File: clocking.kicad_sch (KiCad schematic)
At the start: 10 parts, among them J14 LOCTL, J15 RAMPCTL, Q1 DTC143Z

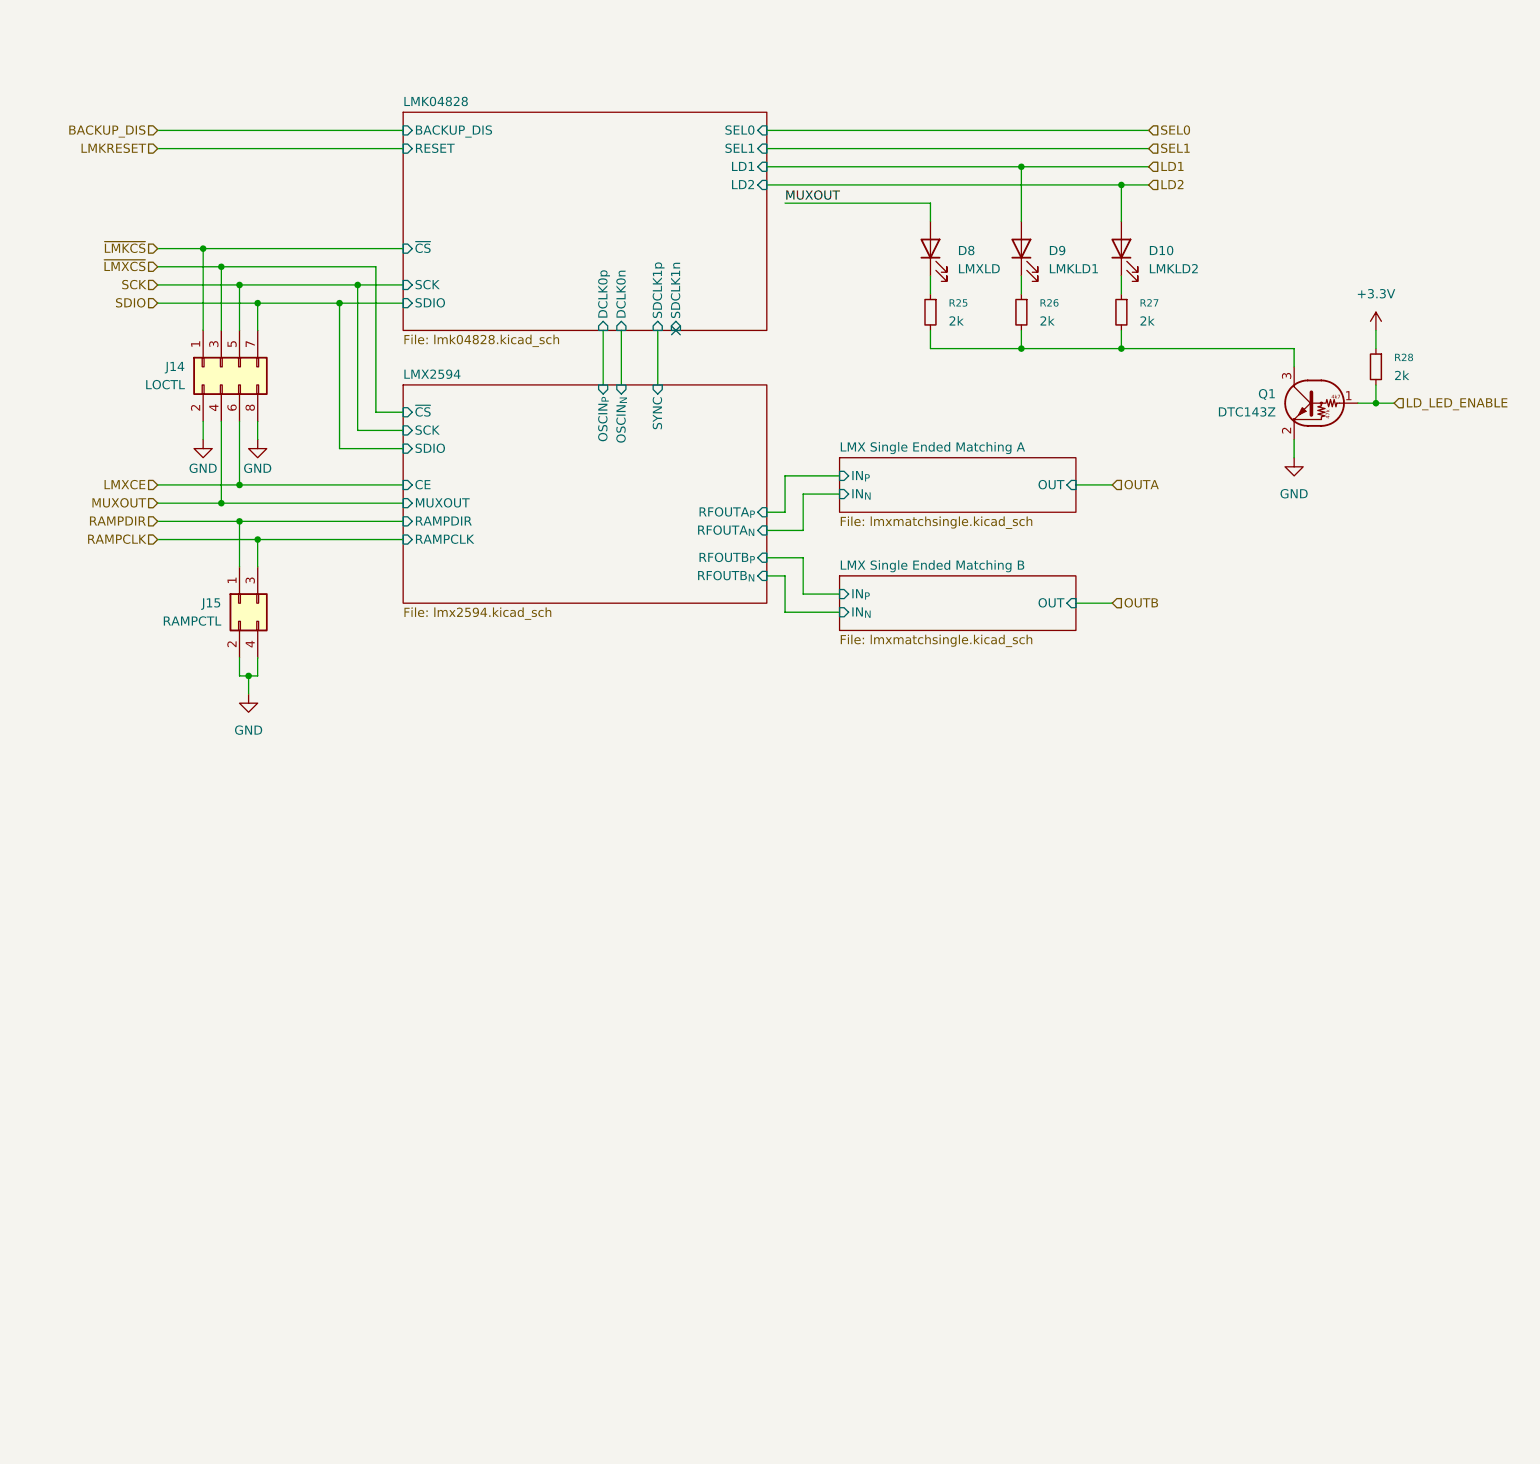
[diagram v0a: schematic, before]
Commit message: Add Clock sources and monitor output
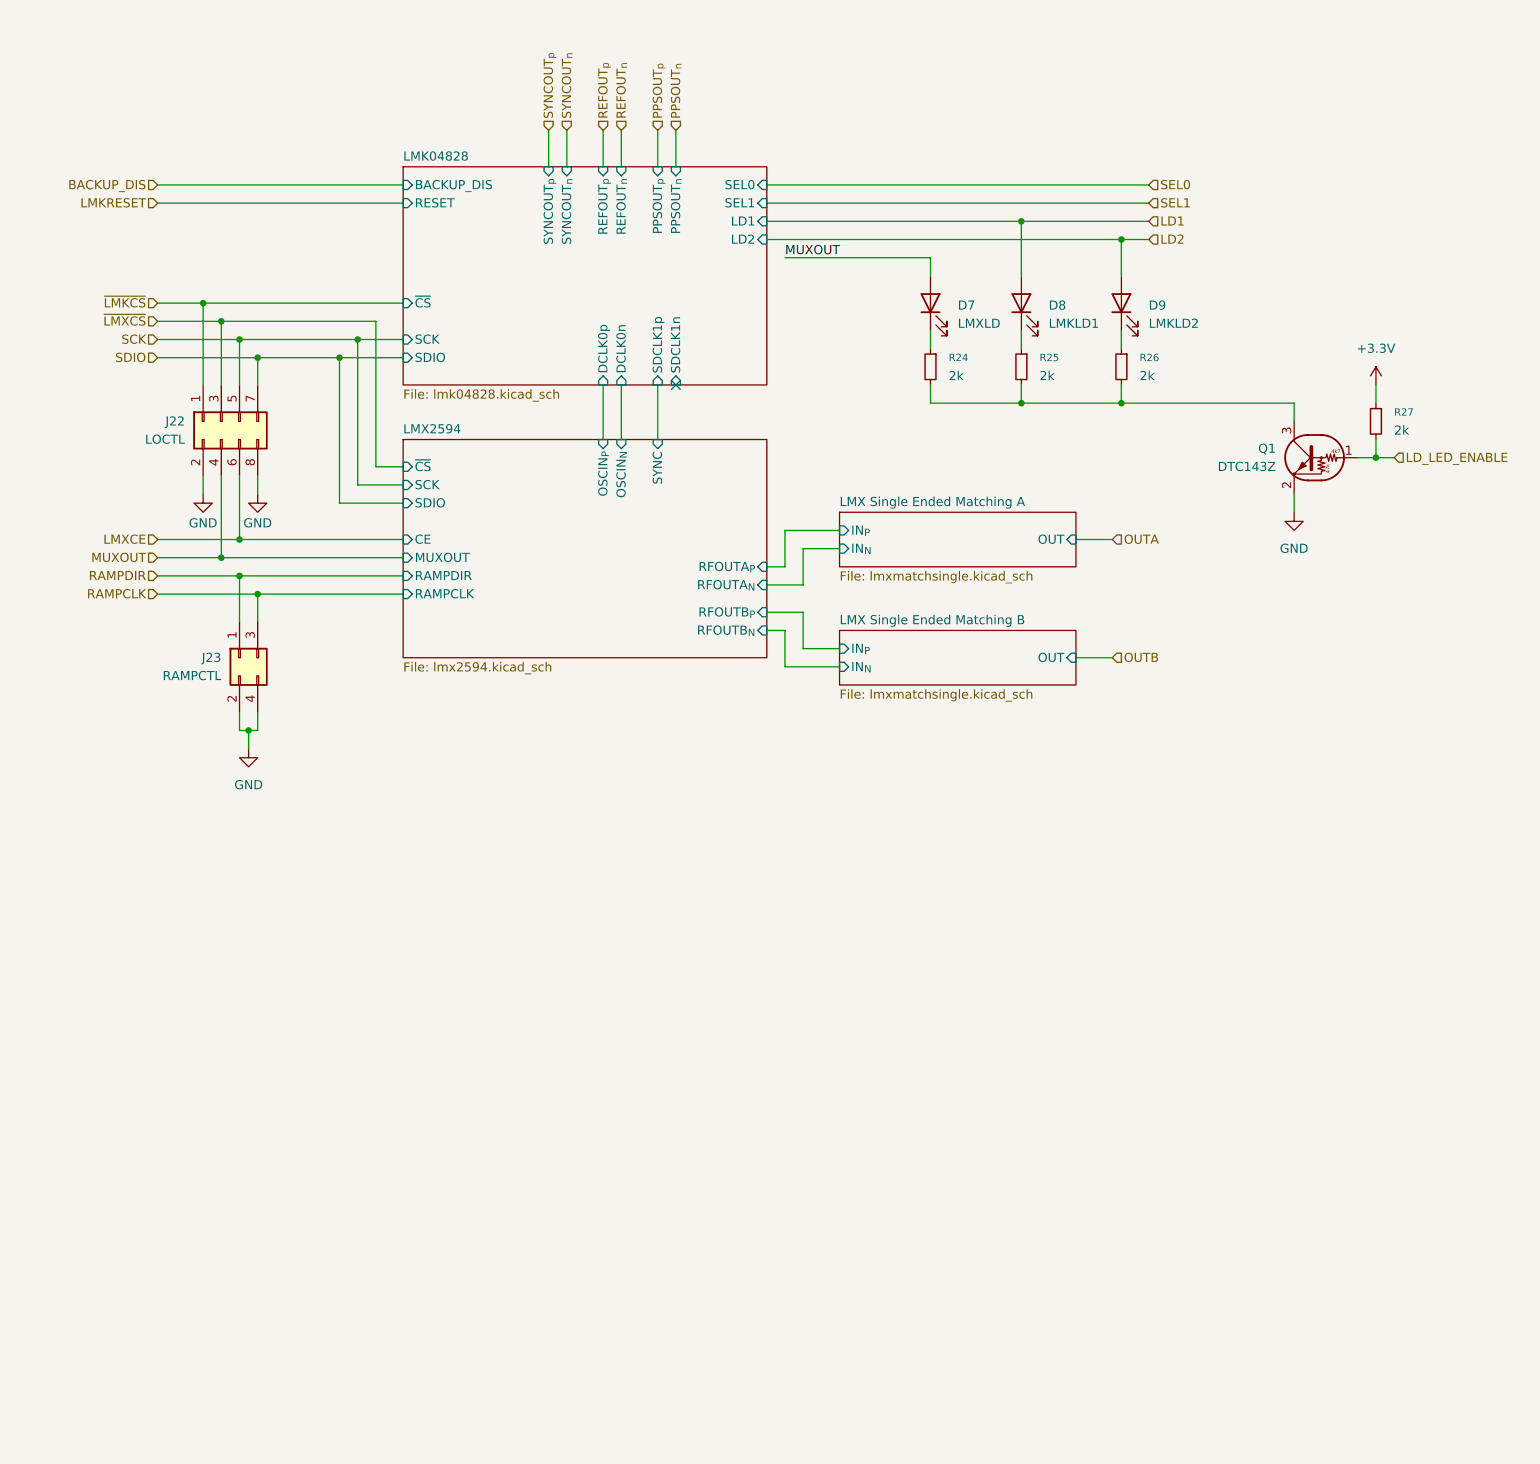
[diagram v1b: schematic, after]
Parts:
- renumbered D8 to D7, D9 to D8, D10 to D9, J14 to J22, J15 to J23, R25 to R24, R26 to R25, R27 to R26, R28 to R27
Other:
- sheet LMK04828 ports: added PPSOUT_{n}, PPSOUT_{p}, REFOUT_{n}, REFOUT_{p}, SYNCOUT_{n}, SYNCOUT_{p}; removed none
- moved on the sheet: D7, D8, D9, J22, J23, Q1, R24, R25, R26, R27

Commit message: Round 1 review comments
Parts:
- renumbered J22 to J23, J23 to J24, R24 to R52, R25 to R53, R26 to R54, R27 to R55
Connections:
- no-connect marks 1 -> 5
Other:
- added sheet LMX Single Ended Matching A1 (lmxmatchsingle.kicad_sch)
- added sheet LMX2595 (lmx2594.kicad_sch)
- sheet LMK04828 ports: added DCLK2n, DCLK2p, SDCLK3n, SDCLK3p; removed none
- sheet LMX Single Ended Matching A ports: added +3.3VA_LMXBUF; removed none
- sheet LMX Single Ended Matching B ports: added +3.3VA_LMXBUF; removed none
- sheet LMX2594 ports: added +3.3VA_LMXBUF; removed none
- moved on the sheet: D7, D8, D9, J23, J24, Q1, R52, R53, R54, R55

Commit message: Round 2 Review, power tree cleanup
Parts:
- renumbered J23 to J24, J24 to J25, R52 to R62, R53 to R63, R54 to R64, R55 to R65
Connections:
- no-connect marks 5 -> 6

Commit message: Darrel Suggestions
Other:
- note added: "10-12GHz"
- note added: "5-7GHZ"
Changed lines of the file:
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@@
 	(generator_version "10.0")
 	(paper "A3")
+	(text "10-12GHz"
+		(exclude_from_sim no)
+		(at 171.45 71.374 0)
+		(effects
+			(font
+				(size 1.27 1.27)
+			)
+		)
+	)
+	(text "5-7GHZ"
+		(exclude_from_sim no)
+		(at 168.656 190.754 0)
+		(effects
+			(font
+				(size 1.27 1.27)
+			)
+		)
+	)
+	(text "5-7GHZ"
+		(exclude_from_sim no)
+		(at 168.656 170.434 0)
+		(effects
+			(font
+				(size 1.27 1.27)
+			)
+		)
+	)
 	(junction
 		(at 162.56 180.34)
@@
 		(dnp no)
 		(fields_autoplaced yes)
-		(property "Reference" "#PWR095"
+		(property "Reference" "#PWR097"
 			(at 190.5 181.61 0)
 			(hide yes)
@@
 			(project "huskypointofload"
 				(path "/eb9c972b-d134-41da-be97-ece3f463f7e0/999a5927-21bb-4ea7-ad27-c6446933693a"
-					(reference "#PWR095")
+					(reference "#PWR097")
 					(unit 1)
 				)
@@
 		(in_pos_files yes)
 		(dnp no)
-		(property "Reference" "#PWR092"
+		(property "Reference" "#PWR094"
 			(at 38.1 179.07 0)
 			(hide yes)
@@
 			(project "huskypointofload"
 				(path "/eb9c972b-d134-41da-be97-ece3f463f7e0/999a5927-21bb-4ea7-ad27-c6446933693a"
-					(reference "#PWR092")
+					(reference "#PWR094")
 					(unit 1)
 				)
@@
 		(dnp no)
 		(fields_autoplaced yes)
-		(property "Reference" "#PWR093"
+		(property "Reference" "#PWR095"
 			(at 44.45 214.63 0)
 			(hide yes)
@@
 			(project "huskypointofload"
 				(path "/eb9c972b-d134-41da-be97-ece3f463f7e0/999a5927-21bb-4ea7-ad27-c6446933693a"
-					(reference "#PWR093")
+					(reference "#PWR095")
 					(unit 1)
 				)
@@
 		(in_pos_files yes)
 		(dnp no)
-		(property "Reference" "#PWR094"
+		(property "Reference" "#PWR096"
 			(at 45.72 179.07 0)
 			(hide yes)
@@
 			(project "huskypointofload"
 				(path "/eb9c972b-d134-41da-be97-ece3f463f7e0/999a5927-21bb-4ea7-ad27-c6446933693a"
-					(reference "#PWR094")
+					(reference "#PWR096")
 					(unit 1)
 				)
@@
 		(dnp no)
 		(fields_autoplaced yes)
-		(property "Reference" "#PWR096"
+		(property "Reference" "#PWR098"
 			(at 201.93 161.29 0)
 			(hide yes)
@@
 			(project "huskypointofload"
 				(path "/eb9c972b-d134-41da-be97-ece3f463f7e0/999a5927-21bb-4ea7-ad27-c6446933693a"
-					(reference "#PWR096")
+					(reference "#PWR098")
 					(unit 1)
 				)

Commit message: Passive footprint pass
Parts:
- D7, D8, D9: footprint (none) -> LED_SMD:LED_0402_1005Metric
- R62, R63, R64, R65: footprint (none) -> Resistor_SMD:R_0402_1005Metric
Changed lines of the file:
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@@
 			)
 		)
-		(property "Footprint" ""
+		(property "Footprint" "LED_SMD:LED_0402_1005Metric"
 			(at 139.7 146.05 0)
 			(hide yes)
@@
 			)
 		)
-		(property "Footprint" ""
+		(property "Footprint" "Resistor_SMD:R_0402_1005Metric"
 			(at 139.7 154.94 0)
 			(hide yes)
@@
 			)
 		)
-		(property "Footprint" ""
+		(property "Footprint" "Resistor_SMD:R_0402_1005Metric"
 			(at 166.37 154.94 0)
 			(hide yes)
@@
 			)
 		)
-		(property "Footprint" ""
+		(property "Footprint" "LED_SMD:LED_0402_1005Metric"
 			(at 166.37 146.05 0)
 			(hide yes)
@@
 			)
 		)
-		(property "Footprint" ""
+		(property "Footprint" "LED_SMD:LED_0402_1005Metric"
 			(at 152.4 146.05 0)
 			(hide yes)
@@
 			)
 		)
-		(property "Footprint" ""
+		(property "Footprint" "Resistor_SMD:R_0402_1005Metric"
 			(at 201.93 162.56 0)
 			(hide yes)
@@
 			)
 		)
-		(property "Footprint" ""
+		(property "Footprint" "Resistor_SMD:R_0402_1005Metric"
 			(at 152.4 154.94 0)
 			(hide yes)

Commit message: add NC and fix ERC
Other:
- sheet LMX2595 renamed LMX2594_PARAMP
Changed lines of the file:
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@@
 			(color 0 0 0 0)
 		)
-		(property "Sheetname" "LMX2595"
+		(property "Sheetname" "LMX2594_PARAMP"
 			(at 66.04 64.0584 0)
 			(show_name no)
